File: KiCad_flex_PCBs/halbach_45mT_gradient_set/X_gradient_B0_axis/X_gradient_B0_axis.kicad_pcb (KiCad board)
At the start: 2 copper layers, 225.4 x 125.8 mm, 70 parts, among them J1+ SolderPad, J2- SolderPad

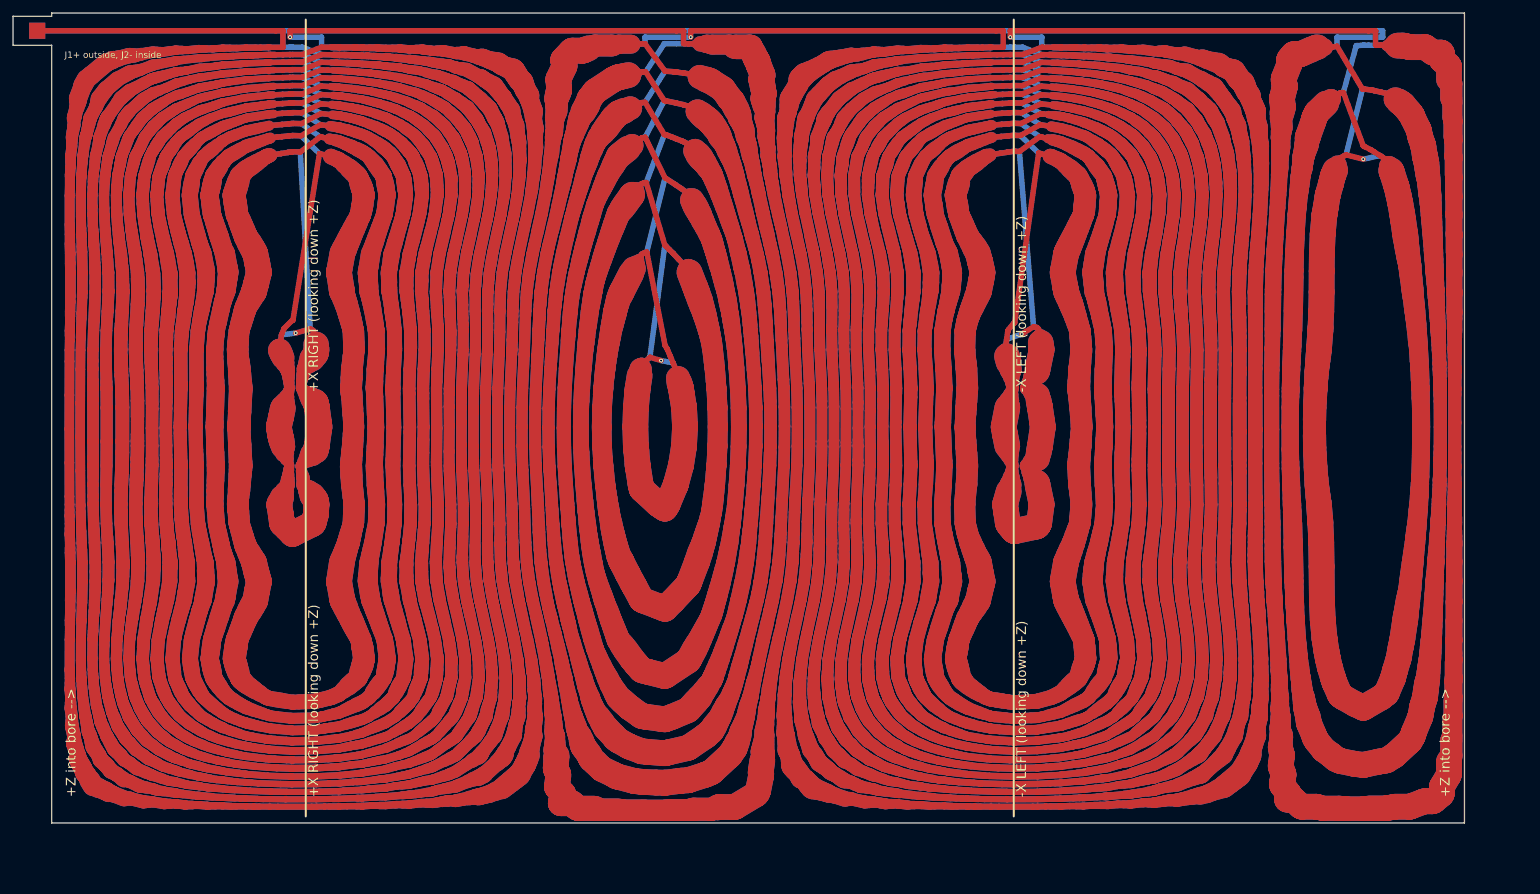
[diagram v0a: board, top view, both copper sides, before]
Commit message: Move the feed tab to the end edge of the flex PCBs
The J1/J2 tab now sticks out past the +axial end of the coil instead of
out of the seam, so the rolled seam is clean and there is room to solder
the leads. Feed and return run as a stacked F.Cu/B.Cu pair along the seam
edge to the routing channel. Larger pads (3 mm) on a 10 mm tab. The tabs
of the three coils sit at their seams: 12, 1 and 6 o'clock looking down +Z.
All boards: DRC clean, same-net gap >= 0.15 mm, re-simulation unchanged.

Co-Authored-By: Claude Opus 5.5 <noreply@anthropic.com>
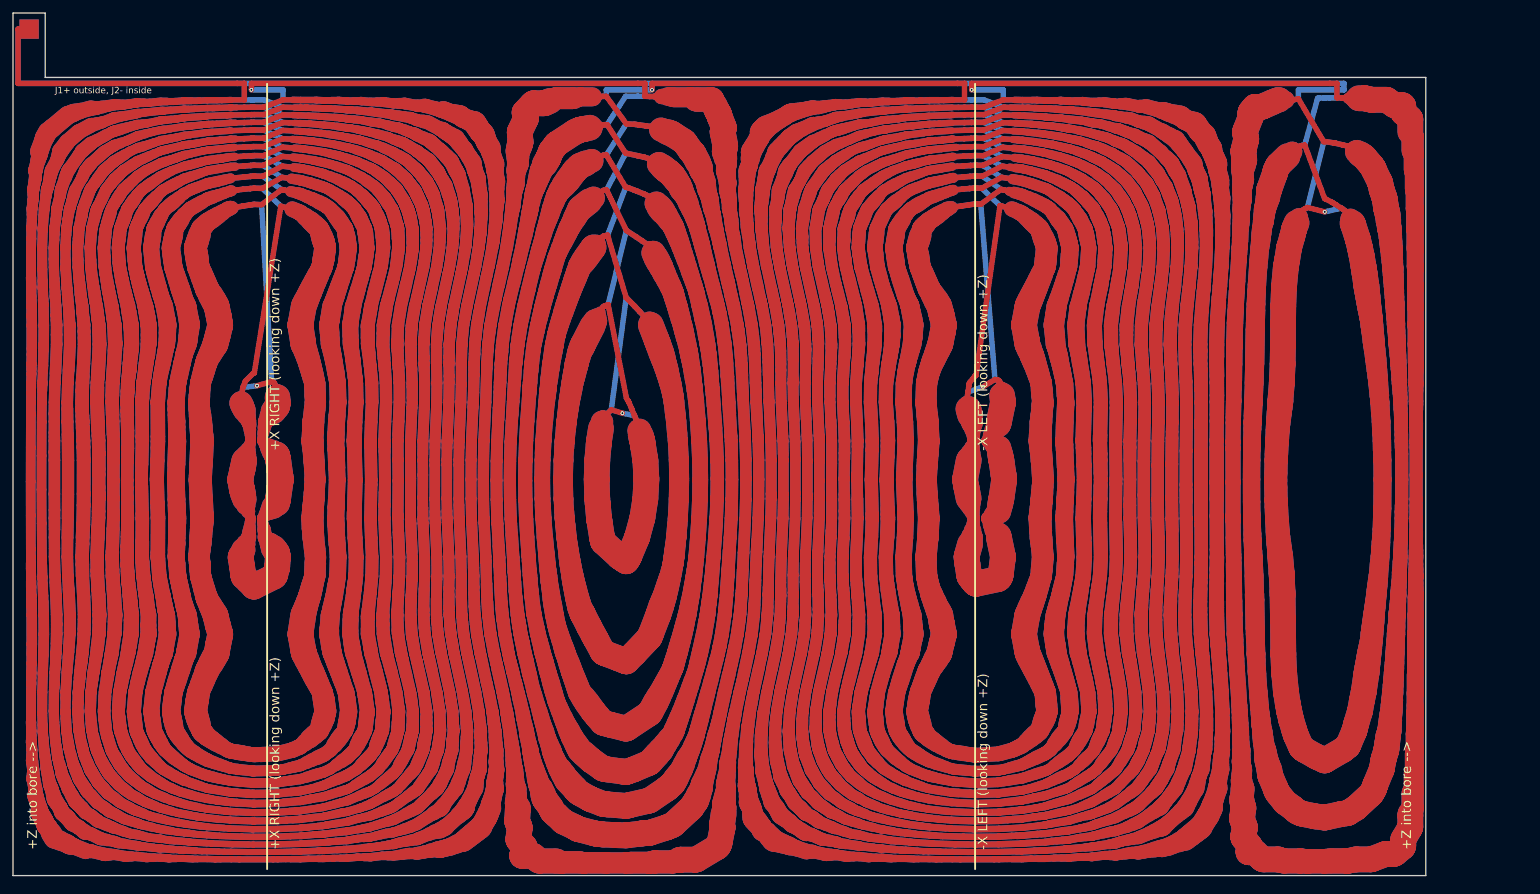
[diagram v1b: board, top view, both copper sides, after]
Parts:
- moved NT11 10.1 mm to (46.8, 37.3)
- moved NT13 10.1 mm to (46.1, 67.2)
- moved NT15 10.1 mm to (46.8, 37.3)
- moved NT29 10.1 mm to (106.9, 37.7)
- moved NT30 10.1 mm to (106.8, 44.8)
- moved NT34 10.1 mm to (106.8, 44.8)
- moved NT35 10.1 mm to (106.9, 37.7)
- moved NT47 10.1 mm to (158.7, 33.7)
- moved NT51 10.1 mm to (158.5, 67.8)
- moved NT55 10.1 mm to (158.7, 33.7)
- moved NT1 10.1 mm to (44.8, 20.9)
- moved NT10 10.1 mm to (46.9, 35.4)
- moved NT12 10.1 mm to (46.7, 39.8)
- moved NT14 10.1 mm to (46.7, 39.8)
- moved NT16 10.1 mm to (46.9, 35.4)
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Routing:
- net COIL_A: track 37.1 -> 44.2 mm
- net G4_B1: track 494.1 -> 501.2 mm
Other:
- board size 225.4 x 125.8 mm -> 219.4 x 134 mm

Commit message: Add JLCPCB flex fab profile, stackup, fab checks and board check script
- KiCad_flex_PCBs/fab_profiles/jlcpcb_flex_2layer_1oz_25um_0p2mm.json:
  JLCPCB 2-layer flex (1 oz, 25 um PI, 0.2 mm) stackup, manufacturer
  limits and the design values used.
- export_kicad_flex_pcb 'fab_profile': design values, layer spacing
  (0.06 mm), KiCad stackup (coverlay, Cu, PI, ENIG, 0.2 mm), coverlay
  opening (0.1 mm) and .kicad_pro rules from the profile; every board is
  checked against the limits (report.fab_check).
- check_kicad_flex_pcb / Examples/check_flex_pcb_boards.m: independent
  checks on the board files (KiCad DRC, same-net clearance, manufacturer
  limits, full-width field).
- Boards regenerated: DRC clean, same-net gap >= 0.15 mm, all JLCPCB
  limits met; gradients 7.34 / 19.49 / 18.86 mT/m/A.
- Documentation of the profile and of all checks.

Co-Authored-By: Claude Opus 5.5 <noreply@anthropic.com>
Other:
- rule pad_to_mask_clearance: 0 -> 0.1000
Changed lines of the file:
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@@
 	(generator_version "1.0")
 	(general
-		(thickness 0.11)
+		(thickness 0.2000)
 		(legacy_teardrops no)
 	)
@@
 		(title "X gradient B0 axis")
 		(comment 1 "F.Cu is the outside of the rolled cylinder; J1/J2 on the tab past the end of the coil")
-		(comment 2 "CoilGen mapping: x0=11.2500 y0=82.4587 layer_gap=0.1000")
+		(comment 2 "CoilGen mapping: x0=11.2500 y0=82.4587 layer_gap=0.0600")
 	)
 	(layers
@@
 	)
 	(setup
-		(pad_to_mask_clearance 0)
+		(stackup
+			(layer "F.SilkS"
+				(type "Top Silk Screen")
+			)
+			(layer "F.Mask"
+				(type "Top Solder Mask")
+				(color "Yellow")
+				(thickness 0.0500)
+				(material "Polyimide coverlay (PI 25 um + adhesive 25 um)")
+			)
+			(layer "F.Cu"
+				(type "copper")
+				(thickness 0.0350)
+			)
+			(layer "dielectric 1"
+				(type "core")
+				(thickness 0.0250)
+				(material "Polyimide")
+				(epsilon_r 3.5)
+				(loss_tangent 0.002)
+			)
+			(layer "B.Cu"
+				(type "copper")
+				(thickness 0.0350)
+			)
+			(layer "B.Mask"
+				(type "Bottom Solder Mask")
+				(color "Yellow")
+				(thickness 0.0500)
+				(material "Polyimide coverlay (PI 25 um + adhesive 25 um)")
+			)
+			(layer "B.SilkS"
+				(type "Bottom Silk Screen")
+			)
+			(copper_finish "ENIG")
+			(dielectric_constraints no)
+		)
+		(pad_to_mask_clearance 0.1000)
 		(allow_soldermask_bridges_in_footprints no)
 	)

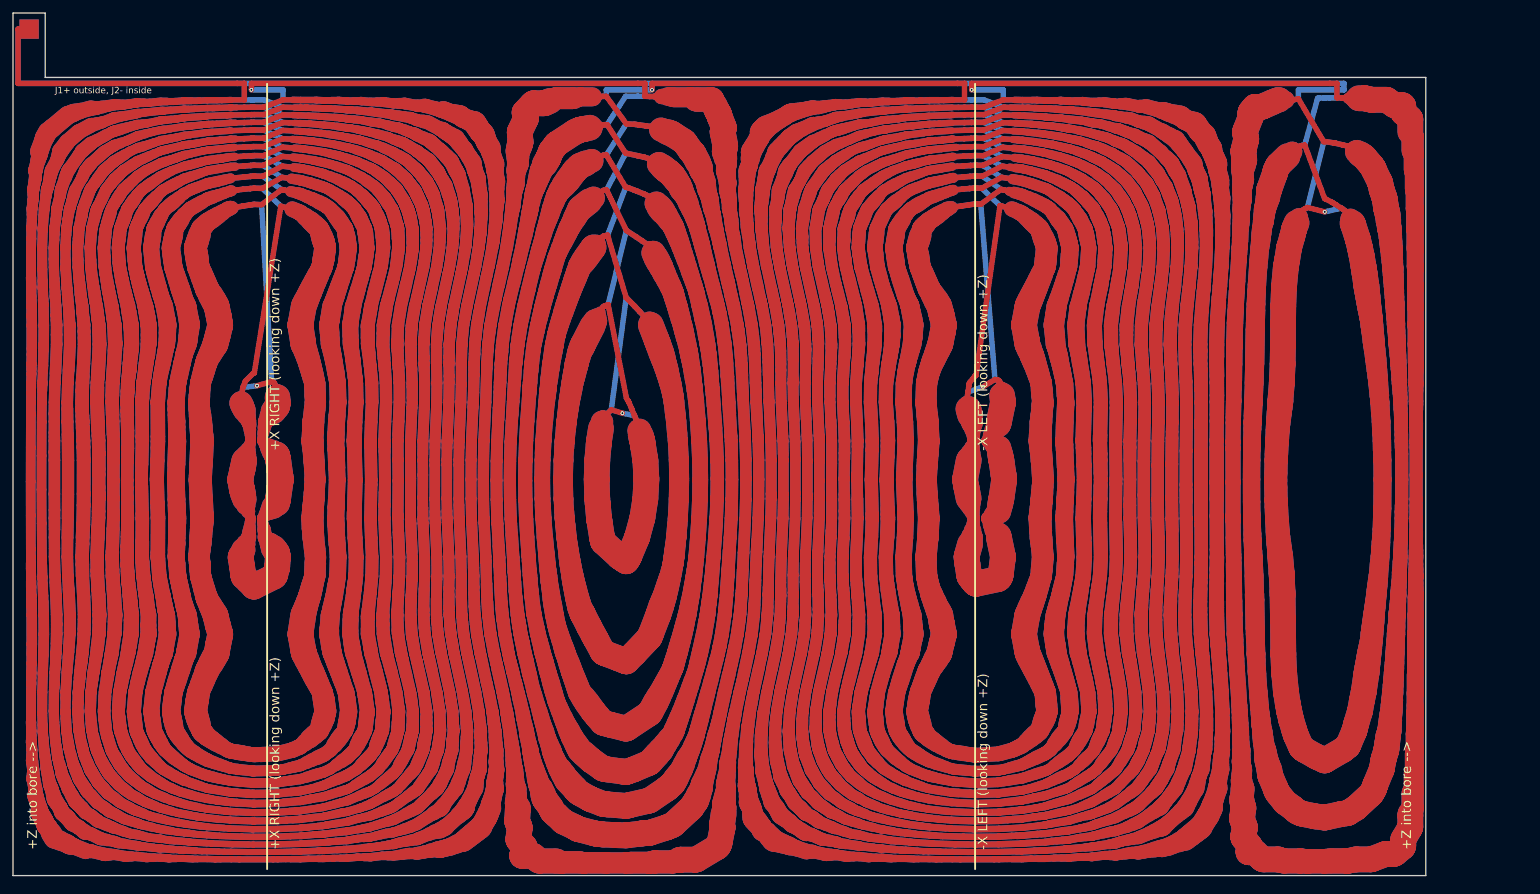
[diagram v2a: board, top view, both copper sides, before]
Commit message: Regenerate the gradient set at 65 / 70 / 75 mm, 120 mm long
- Coils now rolled at 65 (Z), 70 (Y) and 75 mm (X), 120 mm long.
  Z 7.34 mT/m/A, 4.23 ohm, 72 uH, 3.81 A at 28 mT/m (~18.8 V);
  Y 17.9 mT/m/A, 5.05 ohm, 139 uH; X 14.0 mT/m/A, 3.73 ohm, 115 uH.
- All boards: KiCad DRC clean, same-net gap >= 0.15 mm, all JLCPCB
  limits met, re-simulation from the board files matches the design,
  full-width traces change the field by < 0.05 %.
- STEP models and renders regenerated; docs list the tab and seam angles
  and the 24 V check.
- run_kicad_cli: kicad-cli is started with Java's ProcessBuilder and a
  time limit, because MATLAB's system() hangs on macOS after longer
  child processes (STEP export, DRC).

Co-Authored-By: Claude Opus 5.5 <noreply@anthropic.com>
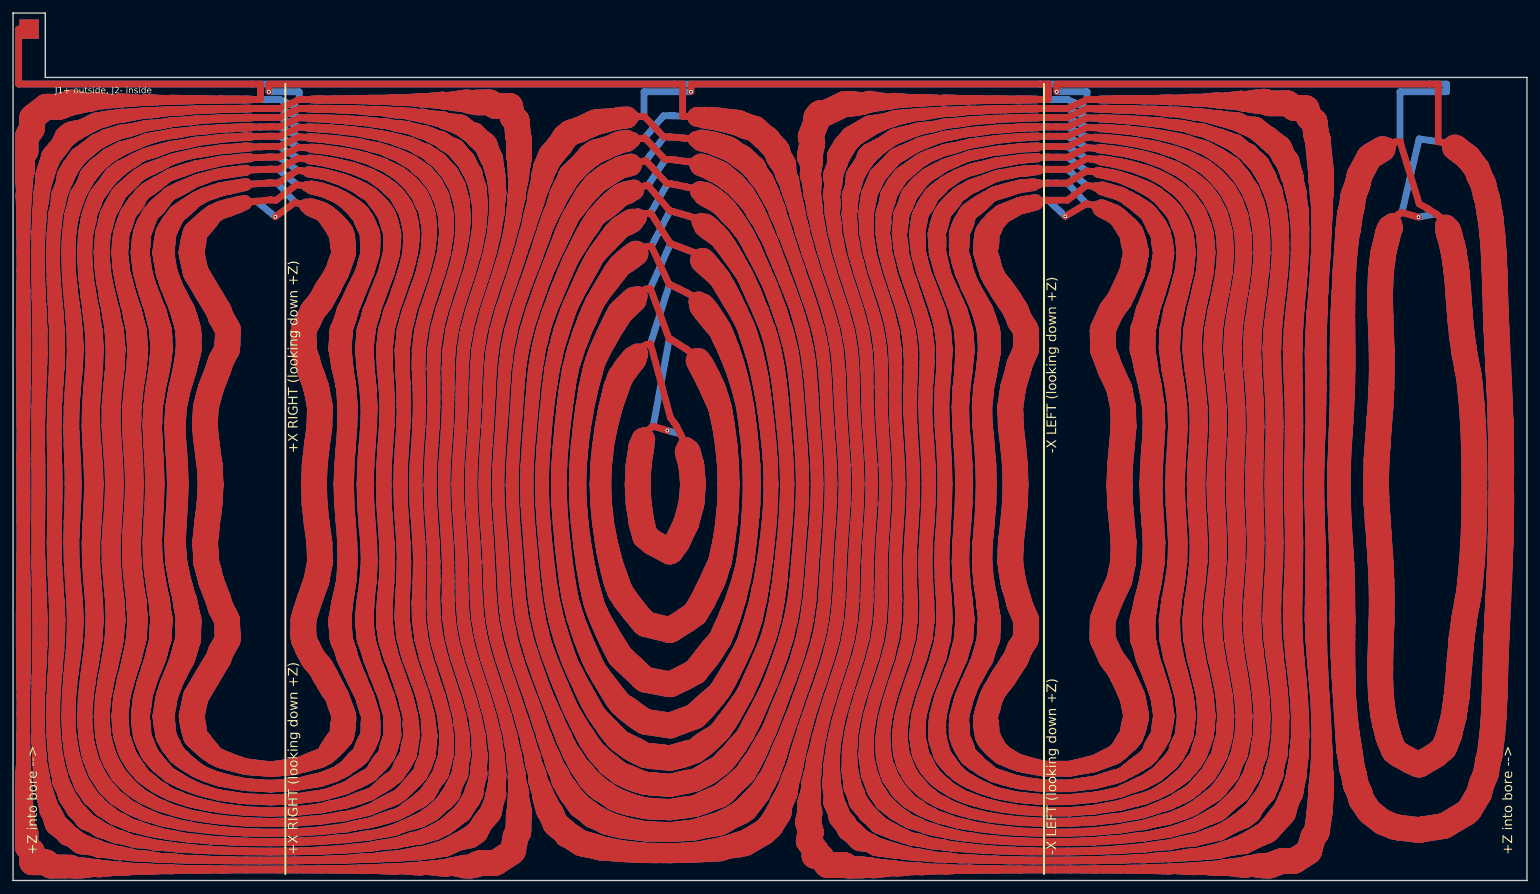
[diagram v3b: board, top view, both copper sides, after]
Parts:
- removed NT59, NT60, NT61, NT62, NT63, NT64, NT65, NT66, NT67, NT68: NetTie, CoilGen:NetTie_Turn
- NT11, NT12, NT13, NT29, NT30, NT31, NT32, NT47, NT48, NT49, NT50, NT51: moved to B.Cu
- NT20, NT21, NT22, NT23, NT24, NT25, NT37, NT38, NT56, NT57: moved to F.Cu
- moved NT56 72.2 mm to (230.0, 21.0)
- moved NT57 71.8 mm to (229.9, 40.5)
- moved NT58 71.2 mm to (230.1, 29.8)
- moved NT25 70.5 mm to (113.7, 46.4)
- moved NT24 68.7 mm to (113.7, 41.2)
- moved NT23 67.2 mm to (113.3, 36.7)
- moved NT20 66.2 mm to (112.7, 21.0)
- moved NT22 66.2 mm to (113.0, 32.8)
- moved NT21 65.8 mm to (112.8, 29.3)
- moved NT38 65.1 mm to (172.1, 24.8)
- moved NT37 62.7 mm to (169.5, 21.0)
- moved NT28 42.5 mm to (113.1, 74.2)
- moved NT51 41.0 mm to (172.1, 29.1)
- moved NT13 35.0 mm to (49.6, 32.4)
- moved NT27 34.6 mm to (113.4, 61.4)
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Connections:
- NT11 pad 2: G1_T11 -> G1_B9
- NT12 pad 1: G1_T11 -> G1_B9
- NT12 pad 2: G1_T12 -> G1_B8
- NT13 pad 1: G1_T12 -> G1_B8
- NT13 pad 2: G1_T13 -> G1_B7
- NT14 pad 1: G1_T13 -> G1_B7
- NT14 pad 2: G1_B12 -> G1_B6
- NT15 pad 1: G1_B12 -> G1_B6
- NT15 pad 2: G1_B11 -> G1_B5
- NT16 pad 1: G1_B11 -> G1_B5
- NT16 pad 2: G1_B10 -> G1_B4
- NT17 pad 1: G1_B10 -> G1_B4
- NT17 pad 2: G1_B9 -> G1_B3
- NT18 pad 1: G1_B9 -> G1_B3
- NT18 pad 2: G1_B8 -> G1_B2
- NT19 pad 1: G1_B8 -> G1_B2
- NT19 pad 2: G1_B7 -> G1_B1
- NT20 pad 1: G1_B7 -> G1_B1
- NT20 pad 2: G1_B6 -> G2_T1
- NT21 pad 1: G1_B6 -> G2_T1
- NT21 pad 2: G1_B5 -> G2_T2
- NT22 pad 1: G1_B5 -> G2_T2
- NT22 pad 2: G1_B4 -> G2_T3
- NT23 pad 1: G1_B4 -> G2_T3
- NT23 pad 2: G1_B3 -> G2_T4
- NT24 pad 1: G1_B3 -> G2_T4
- NT24 pad 2: G1_B2 -> G2_T5
- NT25 pad 1: G1_B2 -> G2_T5
- NT25 pad 2: G1_B1 -> G2_T6
- NT26 pad 1: G1_B1 -> G2_T6
- NT26 pad 2: G2_T1 -> G2_T7
- NT27 pad 1: G2_T1 -> G2_T7
- NT27 pad 2: G2_T2 -> G2_T8
- NT28 pad 1: G2_T2 -> G2_T8
- NT28 pad 2: G2_T3 -> G2_T9
- NT29 pad 1: G2_T3 -> G2_T9
- NT29 pad 2: G2_T4 -> G2_B8
- NT30 pad 1: G2_T4 -> G2_B8
- NT30 pad 2: G2_T5 -> G2_B7
- NT31 pad 1: G2_T5 -> G2_B7
- NT31 pad 2: G2_T6 -> G2_B6
- NT32 pad 1: G2_T6 -> G2_B6
- NT32 pad 2: G2_T7 -> G2_B5
- NT33 pad 1: G2_T7 -> G2_B5
- NT33 pad 2: G2_B6 -> G2_B4
- NT34 pad 1: G2_B6 -> G2_B4
- NT34 pad 2: G2_B5 -> G2_B3
- NT35 pad 1: G2_B5 -> G2_B3
- NT35 pad 2: G2_B4 -> G2_B2
- NT36 pad 1: G2_B4 -> G2_B2
- NT36 pad 2: G2_B3 -> G2_B1
- NT37 pad 1: G2_B3 -> G2_B1
- NT37 pad 2: G2_B2 -> G3_T1
- NT38 pad 1: G2_B2 -> G3_T1
- NT38 pad 2: G2_B1 -> G3_T2
- NT39 pad 1: G2_B1 -> G3_T2
- NT39 pad 2: G3_T1 -> G3_T3
- NT40 pad 1: G3_T1 -> G3_T3
- NT40 pad 2: G3_T2 -> G3_T4
- NT41 pad 1: G3_T2 -> G3_T4
- NT41 pad 2: G3_T3 -> G3_T5
- NT42 pad 1: G3_T3 -> G3_T5
- NT42 pad 2: G3_T4 -> G3_T6
- NT43 pad 1: G3_T4 -> G3_T6
- NT43 pad 2: G3_T5 -> G3_T7
- NT44 pad 1: G3_T5 -> G3_T7
- NT44 pad 2: G3_T6 -> G3_T8
- NT45 pad 1: G3_T6 -> G3_T8
- NT45 pad 2: G3_T7 -> G3_T9
- NT46 pad 1: G3_T7 -> G3_T9
- NT46 pad 2: G3_T8 -> G3_T10
- NT47 pad 1: G3_T8 -> G3_T10
- NT47 pad 2: G3_T9 -> G3_B9
- NT48 pad 1: G3_T9 -> G3_B9
- NT48 pad 2: G3_T10 -> G3_B8
- NT49 pad 1: G3_T10 -> G3_B8
- NT49 pad 2: G3_T11 -> G3_B7
- NT50 pad 1: G3_T11 -> G3_B7
- NT50 pad 2: G3_T12 -> G3_B6
- NT51 pad 1: G3_T12 -> G3_B6
- NT51 pad 2: G3_T13 -> G3_B5
- NT52 pad 1: G3_T13 -> G3_B5
- NT52 pad 2: G3_B12 -> G3_B4
- NT53 pad 1: G3_B12 -> G3_B4
- NT53 pad 2: G3_B11 -> G3_B3
- NT54 pad 1: G3_B11 -> G3_B3
- NT54 pad 2: G3_B10 -> G3_B2
- NT55 pad 1: G3_B10 -> G3_B2
- NT55 pad 2: G3_B9 -> G3_B1
- NT56 pad 1: G3_B9 -> G3_B1
- NT56 pad 2: G3_B8 -> G4_T1
- NT57 pad 1: G3_B8 -> G4_T1
- NT57 pad 2: G3_B7 -> G4_T2
- NT58 pad 1: G3_B7 -> G4_T2
- NT58 pad 2: G3_B6 -> G4_B1
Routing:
- net G4_T3: track 375.4 -> 0.00 mm, vias 1 -> 0
- net G1_B10: track 234.9 -> 0.00 mm
- net G4_B2: track 234.3 -> 0.00 mm
- net G3_B10: track 234.1 -> 0.00 mm
- net G3_T12: track 224.8 -> 0.00 mm
- net G1_T12: track 224.3 -> 0.00 mm
- net G1_T11: track 219.8 -> 0.00 mm
- net G1_B11: track 219.5 -> 0.00 mm
- net G3_T11: track 219.3 -> 0.00 mm
- net G3_B11: track 218.9 -> 0.00 mm
- net G3_B12: track 202.1 -> 0.00 mm
- net G1_B12: track 202.1 -> 0.00 mm
- net G1_T10: track 234.9 -> 434.8 mm, vias 0 -> 1
- net G3_T10: track 234.1 -> 433.4 mm, vias 0 -> 1
- net G1_T13: track 174.5 -> 0.00 mm, vias 1 -> 0
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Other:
- board size 219.4 x 134 mm -> 235.1 x 134.7 mm
